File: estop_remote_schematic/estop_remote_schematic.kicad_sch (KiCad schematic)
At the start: 14 parts, among them J1 Power Switch, J2 ESP32 Pins 1-22, J3 ESP32 Pins 23-44, J4 Battery Connector, J5 EStop Button, M1 HC-12, SW1 Channel Selector Encoder

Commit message: started preliminary pcb layout
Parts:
- removed Brd1: OLEDScreen, symbol SSD1306-128x64_OLED:SSD1306
- removed M1: HC-12, HC-12:MA05-1, symbol HC-12:HC-12
- added C1: 0.1uF, symbol Device:C
- added J6: OLed Screen Pins, symbol Connector:Conn_01x04_Socket
- added J7: HC12 Connections, symbol Connector_Generic:Conn_01x05
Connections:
- net +3.3V: now also J6.3 (Pin_3), J7.1 (Pin_1)
- net +6V: now also PowerCapacitor.1, C1.2
- net GND: now also C1.1, J6.4 (Pin_4), J7.2 (Pin_2)
- net HC12_RX: now also J7.3 (Pin_3)
- net HC12_SET: now also J7.5 (Pin_5)
- net HC12_TX: now also J7.4 (Pin_4)
- net SCL: now also J6.2 (Pin_2)
- net SDA: now also J6.1 (Pin_1)
- net at J1.2 (Pin_2), J4.1 (Pin_1): no longer PowerCapacitor.1
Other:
- company: (none) -> RPI Robotics - Collegiate Competition Robotics
- title: (none) -> emergency_stop_remote
- moved on the sheet: J1, PowerCapacitor

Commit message: updated footprints, cleaned up global labels and updated preliminary PCB to be more accurate
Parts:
- removed SW1: Channel Selector Encoder, symbol Device:RotaryEncoder_Switch
- added C2, C5: 0.1uF, Capacitor_SMD:C_0603_1608Metric_Pad1.08x0.95mm_HandSolder, symbol Device:C
- added J8: Reset Button, Connector_JST:JST_XH_S2B-XH-A_1x02_P2.50mm_Horizontal, symbol Connector_Generic:Conn_01x02
- added SW2: RotaryEncoder_Switch_MP, Rotary_Encoder:RotaryEncoder_Alps_EC11E-Switch_Vertical_H20mm, symbol Device:RotaryEncoder_Switch_MP
- C1: footprint (none) -> Capacitor_SMD:C_0603_1608Metric_Pad1.08x0.95mm_HandSolder
- HC12Capacitor1: renamed from HC12Capacitor; footprint (none) -> Capacitor_THT:CP_Radial_D10.0mm_P5.00mm
- J1, J4, J5: footprint (none) -> Connector_JST:JST_XH_S2B-XH-A_1x02_P2.50mm_Horizontal
- J6: footprint (none) -> Connector_JST:JST_XH_S4B-XH-A_1x04_P2.50mm_Horizontal
- J7: footprint (none) -> holes:2.54mm-5-holes
- PowerCapacitor1: renamed from PowerCapacitor; value 1000uF -> 2200uF; footprint (none) -> Capacitor_THT:CP_Radial_D16.0mm_P7.50mm
- R1, R2: footprint (none) -> Resistor_SMD:R_0805_2012Metric_Pad1.20x1.40mm_HandSolder
- R4, R5: value 220Ω -> 4.7kΩ; footprint (none) -> Resistor_SMD:R_0805_2012Metric_Pad1.20x1.40mm_HandSolder
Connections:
- net +3.3V: now also C2.1
- net BatteryVoltageDivider: now also C5.1
- net ChannelEncoderA: now also SW2.A
- net ChannelEncoderB: now also SW2.B
- net ChannelEncoderSignal: now also SW2.S2
- net GND: now also C2.2, C5.2, J8.2 (Pin_2), SW2.C, SW2.S1
- net Reset: now also J2.3 (Pin_3), J8.1 (Pin_1)
- no-connect marks 0 -> 28
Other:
- note added: "3v3"
- note added: "5V"
- note added: "GND"
- note added: "GPIO0"
- note added: "GPIO1"
- note added: "GPIO10"
- note added: "GPIO11"
- note added: "GPIO12"
- note added: "GPIO13"
- note added: "GPIO14"
- note added: "GPIO15"
- note added: "GPIO16"
- note added: "GPIO17"
- note added: "GPIO18"
- note added: "GPIO2"
- note added: "GPIO20"
- note added: "GPIO21"
- note added: "GPIO3"
- note added: "GPIO35"
- note added: "GPIO36"
- note added: "GPIO37"
- note added: "GPIO38"
- note added: "GPIO39"
- note added: "GPIO4"
- note added: "GPIO40"
- note added: "GPIO41"
- note added: "GPIO42"
- note added: "GPIO45"
- note added: "GPIO46"
- note added: "GPIO47"
- note added: "GPIO48"
- note added: "GPIO5"
- note added: "GPIO6"
- note added: "GPIO7"
- note added: "GPIO8"
- note added: "GPIO9"
- note added: "RESET"
- note added: "RX"
- note added: "TX"
- moved on the sheet: HC12Capacitor1, R1, R2

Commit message: added initial PCB cut edges
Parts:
- HC12Capacitor1: footprint Capacitor_THT:CP_Radial_D10.0mm_P5.00mm -> Capacitor_THT:CP_Radial_D7.5mm_P2.50mm
- J1: footprint Connector_JST:JST_XH_S2B-XH-A_1x02_P2.50mm_Horizontal -> Connector_JST:JST_XH_B2B-XH-AM_1x02_P2.50mm_Vertical
- J4, J5, J8: footprint Connector_JST:JST_XH_S2B-XH-A_1x02_P2.50mm_Horizontal -> Connector_JST:JST_XH_B2B-XH-A_1x02_P2.50mm_Vertical
- J6: footprint Connector_JST:JST_XH_S4B-XH-A_1x04_P2.50mm_Horizontal -> Connector_JST:JST_XH_S4B-XH-A-1_1x04_P2.50mm_Horizontal
- J7: footprint holes:2.54mm-5-holes -> Connector_PinHeader_2.54mm:PinHeader_1x05_P2.54mm_Vertical
- PowerCapacitor1: footprint Capacitor_THT:CP_Radial_D16.0mm_P7.50mm -> Capacitor_THT:CP_Radial_D10.0mm_P5.00mm
- renumbered C5 to ADCDecouplingCapacitor1, C2 to HC12DecouplingCapacitor1, R5 to I2CPullup1, R4 to I2CPullup2, C1 to PowerCapacitor2, R1 to VoltDivResistor1, R2 to VoltDivResistor2
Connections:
- net +6V: now also J1.2 (Pin_2), J2.21 (Pin_21); no longer J1.1 (Pin_1)
- net at J4.1 (Pin_1): now also J1.1 (Pin_1); no longer J1.2 (Pin_2)
- no-connect marks 28 -> 27
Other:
- moved on the sheet: J1
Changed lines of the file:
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@@
 	)
 	(no_connect
-		(at 231.14 156.21)
-	)
-	(no_connect
 		(at 231.14 151.13)
 	)
@@
 	(wire
 		(pts
+			(xy 63.5 27.94) (xy 63.5 34.29)
+		)
+		(stroke
+			(width 0)
+			(type default)
+		)
+	)
+	(wire
+		(pts
 			(xy 43.18 20.32) (xy 43.18 21.59)
 		)
@@
 	(wire
 		(pts
+			(xy 71.12 27.94) (xy 71.12 34.29)
+		)
+		(stroke
+			(width 0)
+			(type default)
+		)
+	)
+	(wire
+		(pts
 			(xy 25.4 137.16) (xy 66.04 137.16)
 		)
@@
 	(wire
 		(pts
-			(xy 68.58 34.29) (xy 74.93 34.29)
+			(xy 68.58 27.94) (xy 71.12 27.94)
 		)
 		(stroke
@@
 	(wire
 		(pts
+			(xy 63.5 34.29) (xy 53.34 34.29)
+		)
+		(stroke
+			(width 0)
+			(type default)
+		)
+	)
+	(wire
+		(pts
 			(xy 241.3 35.56) (xy 254 35.56)
 		)
@@
 	(wire
 		(pts
-			(xy 53.34 34.29) (xy 66.04 34.29)
+			(xy 63.5 27.94) (xy 66.04 27.94)
 		)
 		(stroke
@@
 	(wire
 		(pts
+			(xy 71.12 34.29) (xy 74.93 34.29)
+		)
+		(stroke
+			(width 0)
+			(type default)
+		)
+	)
+	(wire
+		(pts
 			(xy 25.4 139.7) (xy 66.04 139.7)
 		)
@@
 		(dnp no)
 		(fields_autoplaced yes)
-		(property "Reference" "R5"
+		(property "Reference" "I2CPullup1"
 			(at 35.56 186.6899 0)
 			(show_name no)
@@
 			(project "estop_remote_schematic"
 				(path "/5c08b7c6-3fe1-4a20-81ff-6cf06621ce55"
-					(reference "R5")
+					(reference "I2CPullup1")
 					(unit 1)
 				)
@@
 		(dnp no)
 		(fields_autoplaced yes)
-		(property "Reference" "C5"
+		(property "Reference" "ADCDecouplingCapacitor1"
 			(at 58.42 53.3399 0)
 			(show_name no)
@@
 			(project "estop_remote_schematic"
 				(path "/5c08b7c6-3fe1-4a20-81ff-6cf06621ce55"
-					(reference "C5")
+					(reference "ADCDecouplingCapacitor1")
+					(unit 1)
+				)
+			)
+		)
+	)
+	(symbol
+		(lib_id "power:+6V")
+		(at 231.14 156.21 90)
+		(unit 1)
+		(body_style 1)
+		(exclude_from_sim no)
+		(in_bom yes)
+		(on_board yes)
+		(in_pos_files yes)
+		(dnp no)
+		(fields_autoplaced yes)
+		(property "Reference" "#PWR021"
+			(at 234.95 156.21 0)
+			(hide yes)
+			(show_name no)
+			(do_not_autoplace no)
+			(effects
+				(font
+					(size 1.27 1.27)
+				)
+			)
+		)
+		(property "Value" "+6V"
+			(at 227.33 156.2099 90)
+			(show_name no)
+			(do_not_autoplace no)
+			(effects
+				(font
+					(size 1.27 1.27)
+				)
+				(justify left)
+			)
+		)
+		(property "Footprint" ""
+			(at 231.14 156.21 0)
+			(hide yes)
+			(show_name no)
+			(do_not_autoplace no)
+			(effects
+				(font
+					(size 1.27 1.27)
+				)
+			)
+		)
+		(property "Datasheet" ""
+			(at 231.14 156.21 0)
+			(hide yes)
+			(show_name no)
+			(do_not_autoplace no)
+			(effects
+				(font
+					(size 1.27 1.27)
+				)
+			)
+		)
+		(property "Description" "Power symbol creates a global label with name \"+6V\""
+			(at 231.14 156.21 0)
+			(hide yes)
+			(show_name no)
+			(do_not_autoplace no)
+			(effects
+				(font
+					(size 1.27 1.27)
+				)
+			)
+		)
+		(pin "1"
+		)
+		(instances
+			(project "estop_remote_schematic"
+				(path "/5c08b7c6-3fe1-4a20-81ff-6cf06621ce55"
+					(reference "#PWR021")
 					(unit 1)
 				)
@@
 	(symbol
 		(lib_id "Connector_Generic:Conn_01x02")
-		(at 66.04 29.21 90)
+		(at 68.58 33.02 270)
 		(unit 1)
 		(body_style 1)
@@
 		(dnp no)
 		(property "Reference" "J1"
-			(at 66.04 24.13 90)
+			(at 68.072 26.67 90)
 			(show_name no)
 			(do_not_autoplace no)
@@
 		)
 		(property "Value" "Power Switch"
-			(at 60.452 26.416 90)
+			(at 73.914 24.13 90)
 			(show_name no)
 			(do_not_autoplace no)
@@
 			)
 		)
-		(property "Footprint" "Connector_JST:JST_XH_S2B-XH-A_1x02_P2.50mm_Horizontal"
-			(at 66.04 29.21 0)
+		(property "Footprint" "Connector_JST:JST_XH_B2B-XH-AM_1x02_P2.50mm_Vertical"
+			(at 68.58 33.02 0)
 			(hide yes)
 			(show_name no)
@@
 		)
 		(property "Datasheet" ""
-			(at 66.04 29.21 0)
+			(at 68.58 33.02 0)
 			(hide yes)
 			(show_name no)
@@
 		)
 		(property "Description" "Generic connector, single row, 01x02, script generated (kicad-library-utils/schlib/autogen/connector/)"
-			(at 66.04 29.21 0)
+			(at 68.58 33.02 0)
 			(hide yes)
 			(show_name no)
@@
 		(dnp no)
 		(fields_autoplaced yes)
-		(property "Reference" "C2"
+		(property "Reference" "HC12DecouplingCapacitor1"
 			(at 59.69 129.5399 0)
 			(show_name no)
@@
 			(project "estop_remote_schematic"
 				(path "/5c08b7c6-3fe1-4a20-81ff-6cf06621ce55"
-					(reference "C2")
+					(reference "HC12DecouplingCapacitor1")
 					(unit 1)
 				)
@@
 		(dnp no)
 		(fields_autoplaced yes)
-		(property "Reference" "R1"
+		(property "Reference" "VoltDivResistor1"
 			(at 40.64 36.83 90)
 			(show_name no)
@@
 			(project "estop_remote_schematic"
 				(path "/5c08b7c6-3fe1-4a20-81ff-6cf06621ce55"
-					(reference "R1")
+					(reference "VoltDivResistor1")
 					(unit 1)
 				)
@@
 			)
 		)
-		(property "Footprint" "Connector_JST:JST_XH_S2B-XH-A_1x02_P2.50mm_Horizontal"
+		(property "Footprint" "Connector_JST:JST_XH_B2B-XH-A_1x02_P2.50mm_Vertical"
 			(at 254 30.48 0)
 			(hide yes)
@@
 		(in_pos_files yes)
 		(dnp no)
-		(property "Reference" "C1"
-			(at 29.21 28.702 0)
+		(property "Reference" "PowerCapacitor2"
+			(at 17.272 28.448 0)
 			(show_name no)
 			(do_not_autoplace no)
@@
 			(project "estop_remote_schematic"
 				(path "/5c08b7c6-3fe1-4a20-81ff-6cf06621ce55"
-					(reference "C1")
+					(reference "PowerCapacitor2")
 					(unit 1)
 				)
@@
 			)
 		)
-		(property "Footprint" "Connector_JST:JST_XH_S4B-XH-A_1x04_P2.50mm_Horizontal"
+		(property "Footprint" "Connector_JST:JST_XH_S4B-XH-A-1_1x04_P2.50mm_Horizontal"
 			(at 69.85 181.61 0)
 			(hide yes)
@@
 			)
 		)
-		(property "Footprint" "Connector_JST:JST_XH_S2B-XH-A_1x02_P2.50mm_Horizontal"
+		(property "Footprint" "Connector_JST:JST_XH_B2B-XH-A_1x02_P2.50mm_Vertical"
 			(at 254 20.32 0)
 			(hide yes)
@@
 		(dnp no)
 		(fields_autoplaced yes)
-		(property "Reference" "R2"
+		(property "Reference" "VoltDivResistor2"
 			(at 68.58 36.83 90)
 			(show_name no)
@@
 			(project "estop_remote_schematic"
 				(path "/5c08b7c6-3fe1-4a20-81ff-6cf06621ce55"
-					(reference "R2")
+					(reference "VoltDivResistor2")
 					(unit 1)
 				)
@@
 			)
 		)
-		(property "Footprint" "Capacitor_THT:CP_Radial_D10.0mm_P5.00mm"
+		(property "Footprint" "Capacitor_THT:CP_Radial_D7.5mm_P2.50mm"
 			(at 49.2252 134.62 0)
 			(hide yes)
@@
 			)
 		)
-		(property "Footprint" "Connector_JST:JST_XH_S2B-XH-A_1x02_P2.50mm_Horizontal"
+		(property "Footprint" "Connector_JST:JST_XH_B2B-XH-A_1x02_P2.50mm_Vertical"
 			(at 74.93 29.21 0)
 			(hide yes)
@@
 			)
 		)
-		(property "Footprint" "Capacitor_THT:CP_Radial_D16.0mm_P7.50mm"
+		(property "Footprint" "Capacitor_THT:CP_Radial_D10.0mm_P5.00mm"
 			(at 42.2148 26.67 0)
 			(hide yes)
@@
 			)
 		)
-		(property "Footprint" "holes:2.54mm-5-holes"
+		(property "Footprint" "Connector_PinHeader_2.54mm:PinHeader_1x05_P2.54mm_Vertical"
 			(at 71.12 137.16 0)
 			(hide yes)
@@
 		(dnp no)
 		(fields_autoplaced yes)
-		(property "Reference" "R4"
+		(property "Reference" "I2CPullup2"
 			(at 46.99 186.6899 0)
 			(show_name no)
@@
 			(project "estop_remote_schematic"
 				(path "/5c08b7c6-3fe1-4a20-81ff-6cf06621ce55"
-					(reference "R4")
+					(reference "I2CPullup2")
 					(unit 1)
 				)

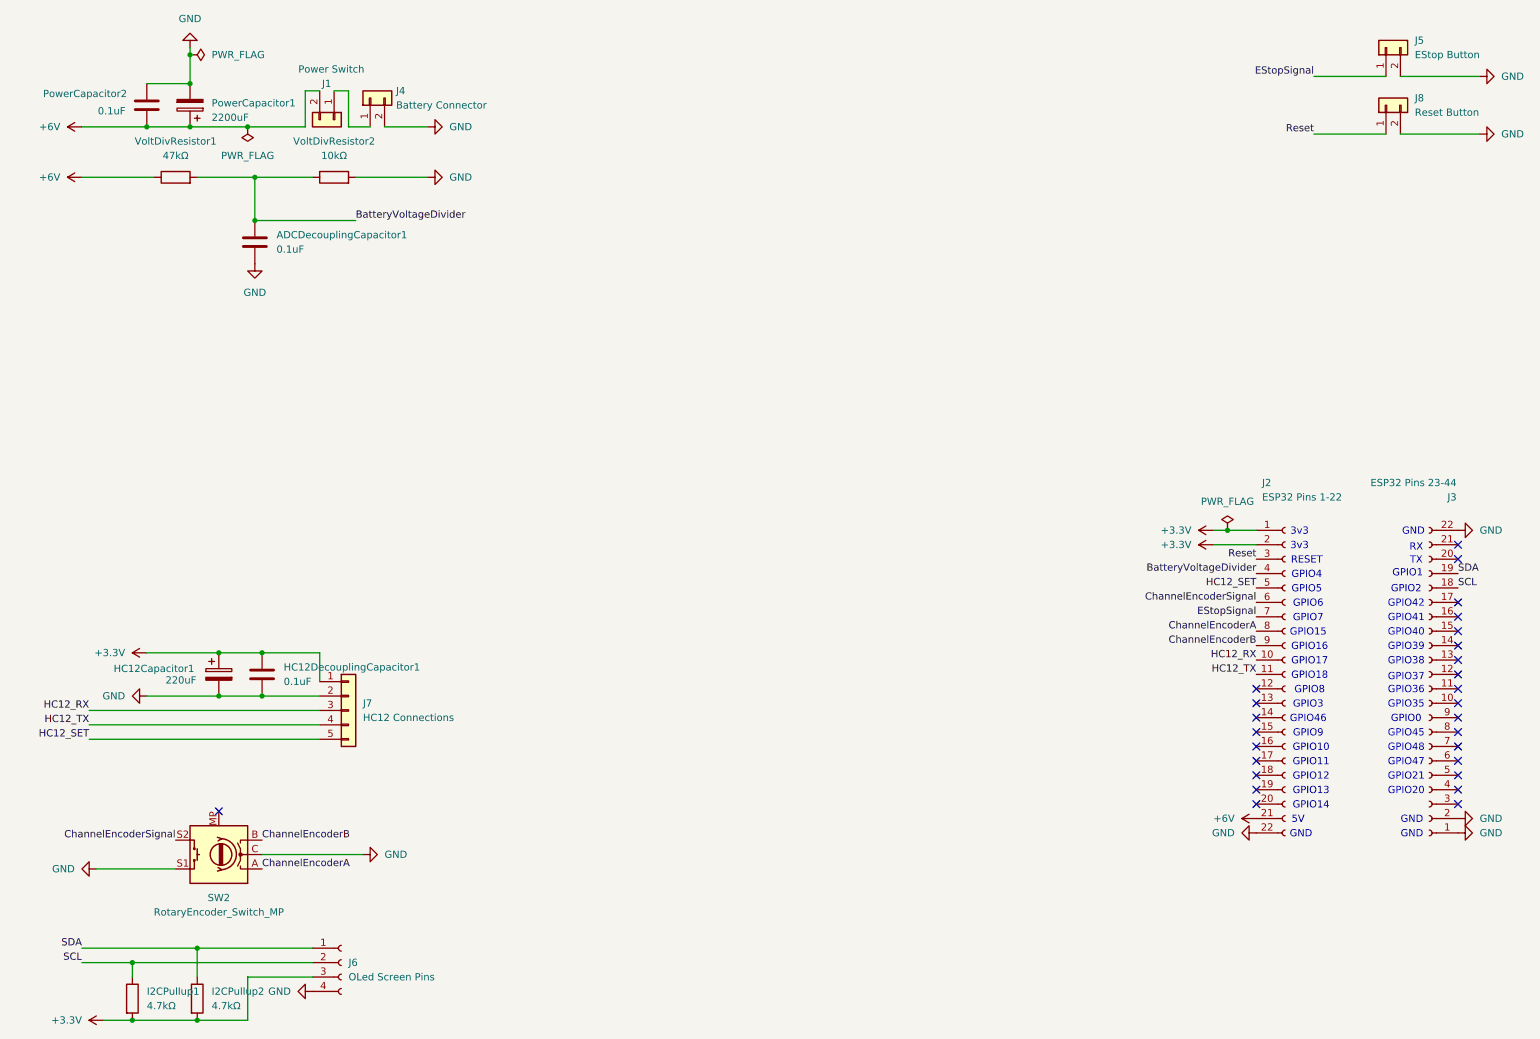
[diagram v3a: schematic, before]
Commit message: Adjusted layout of PCB to shrink size and optimize trace layout
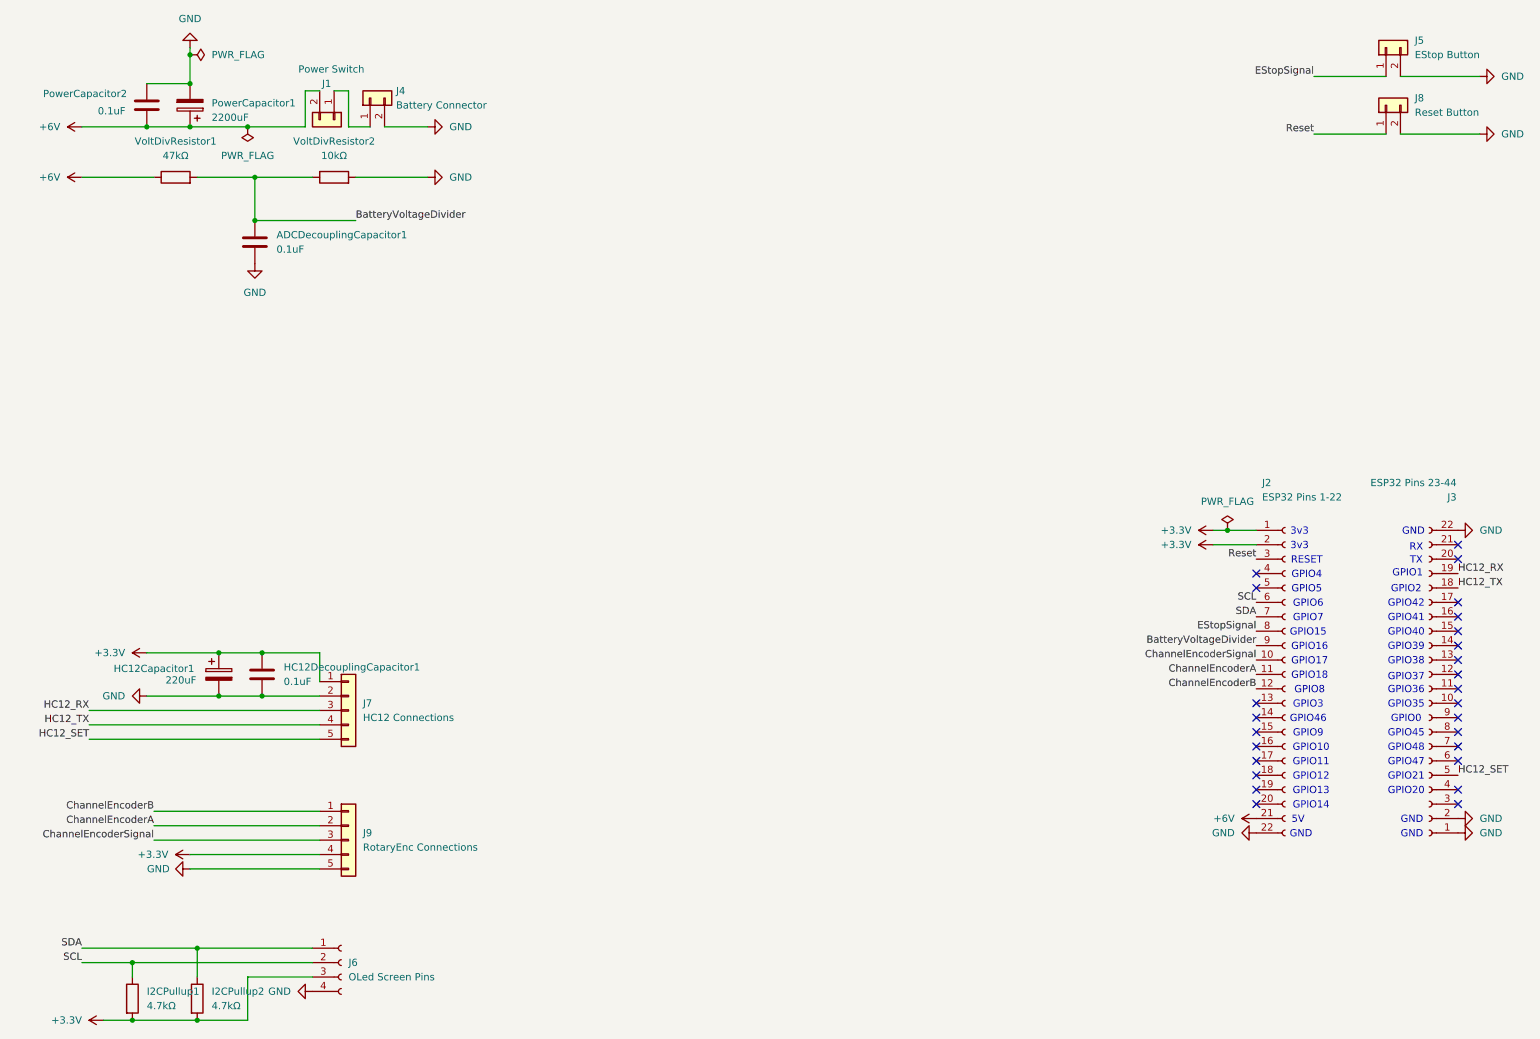
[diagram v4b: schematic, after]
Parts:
- removed SW2: RotaryEncoder_Switch_MP, Rotary_Encoder:RotaryEncoder_Alps_EC11E-Switch_Vertical_H20mm, symbol Device:RotaryEncoder_Switch_MP
- added J9: RotaryEnc Connections, Connector_JST:JST_XH_B5B-XH-A_1x05_P2.50mm_Vertical, symbol Connector_Generic:Conn_01x05
- J1: footprint Connector_JST:JST_XH_B2B-XH-AM_1x02_P2.50mm_Vertical -> Connector_JST:JST_XH_B2B-XH-A_1x02_P2.50mm_Vertical
- J6: footprint Connector_JST:JST_XH_S4B-XH-A-1_1x04_P2.50mm_Horizontal -> Connector_JST:JST_XH_B4B-XH-A_1x04_P2.50mm_Vertical
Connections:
- net +3.3V: now also J9.4 (Pin_4)
- net BatteryVoltageDivider: now also J2.9 (Pin_9); no longer J2.4 (Pin_4)
- net ChannelEncoderA: now also J2.11 (Pin_11), J9.2 (Pin_2); no longer J2.8 (Pin_8)
- net ChannelEncoderB: now also J2.12 (Pin_12), J9.1 (Pin_1); no longer J2.9 (Pin_9)
- net ChannelEncoderSignal: now also J2.10 (Pin_10), J9.3 (Pin_3); no longer J2.6 (Pin_6)
- net EStopSignal: now also J2.8 (Pin_8); no longer J2.7 (Pin_7)
- net GND: now also J9.5 (Pin_5)
- net HC12_RX: now also J3.19 (Pin_19); no longer J2.10 (Pin_10)
- net HC12_SET: now also J3.5 (Pin_5); no longer J2.5 (Pin_5)
- net HC12_TX: now also J3.18 (Pin_18); no longer J2.11 (Pin_11)
- net SCL: now also J2.6 (Pin_6); no longer J3.18 (Pin_18)
- net SDA: now also J2.7 (Pin_7); no longer J3.19 (Pin_19)
- no-connect marks 27 -> 26
